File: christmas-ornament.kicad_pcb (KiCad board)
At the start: 2 copper layers, 76.2 x 76.2 mm, 14 parts, among them SW1 SW_SPDT

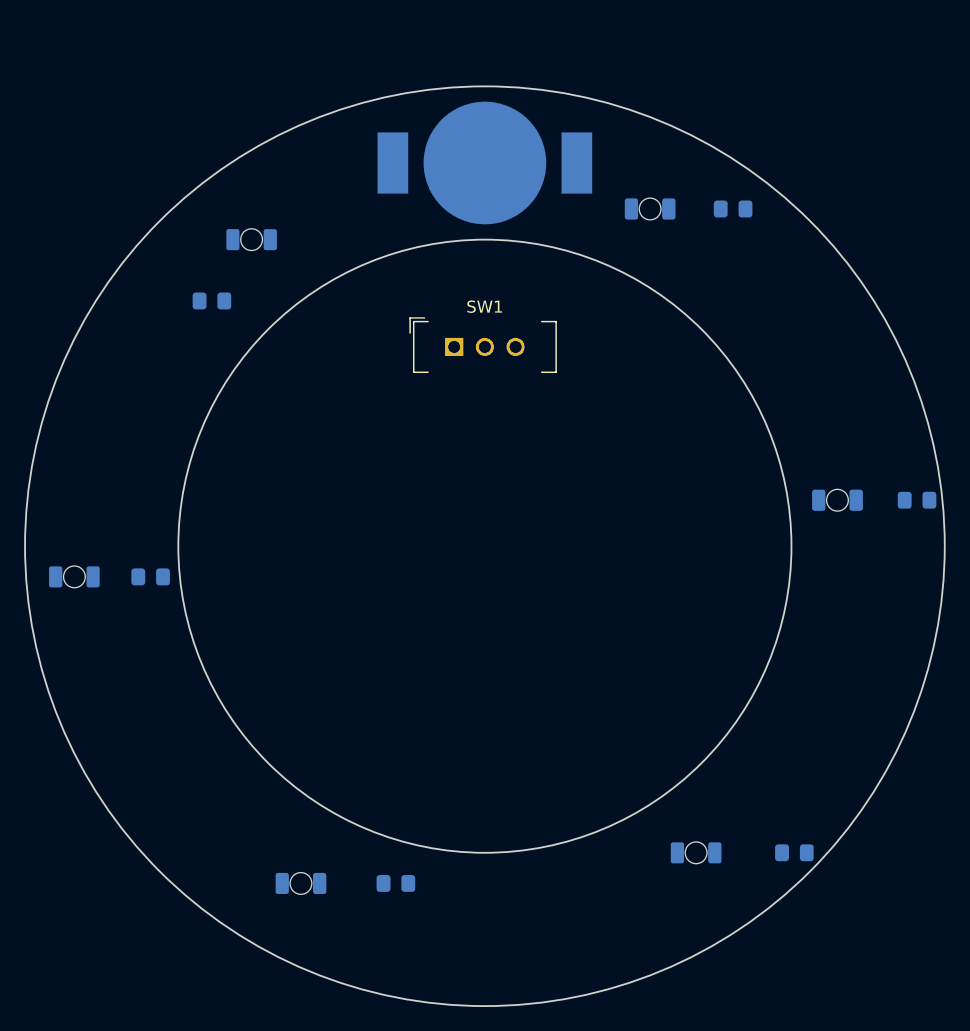
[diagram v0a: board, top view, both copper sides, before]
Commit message: use the square hole led footprint
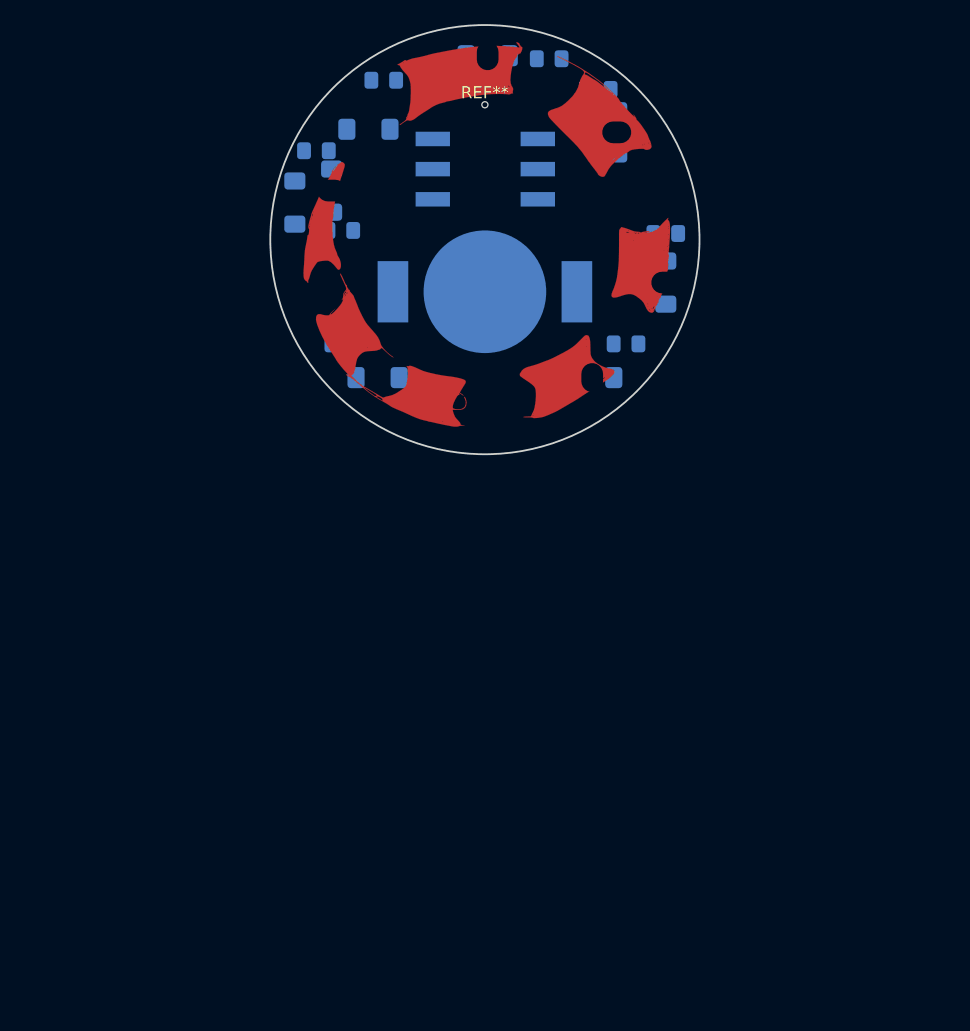
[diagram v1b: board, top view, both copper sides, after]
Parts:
- added D7: LED, salvation:LED_1206_ReverseMountSquare1.5mm_HandSolder, B.Cu at (161.3, 113.0)
- added D8: LED, salvation:LED_1206_ReverseMountSquare1.5mm_HandSolder, B.Cu at (143.5, 113.0)
- added G***: LOGO, salvation:snek, F.Cu at (152.4, 101.6)
- added R7: 68, Resistor_SMD:R_0805_2012Metric_Pad1.15x1.40mm_HandSolder, B.Cu at (164.1, 110.2)
- added R8: 68, Resistor_SMD:R_0805_2012Metric_Pad1.15x1.40mm_HandSolder, B.Cu at (140.7, 110.2)
- added REF**: wire_hole, salvation:wire_hole, F.Cu at (152.4, 90.4)
- D1, D2, D3, D4, D5, D6: footprint salvation:LED_1206_3216Metric_ReverseMount_Hole1.8x2.4mm -> salvation:LED_1206_ReverseMountSquare1.5mm_HandSolder
- SW1: footprint salvation:SW_EG1218_SPDT -> salvation:smd_spdt; moved to B.Cu
- moved R4 68.9 mm to (157.7, 86.6), turned to 180 degrees
- moved D4 68.3 mm to (152.6, 86.4)
- moved R5 67.9 mm to (161.8, 89.2), turned to 180 degrees
- moved D5 67.5 mm to (163.3, 92.7), turned to 90 degrees
- moved R3 56.2 mm to (144.0, 88.4)
- moved D6 54.7 mm to (167.4, 105.2), turned to 90 degrees
- moved R6 51.3 mm to (167.4, 101.1)
- moved D3 49.5 mm to (142.7, 92.5)
- moved R2 32.6 mm to (140.5, 100.8)
- moved D2 26.4 mm to (139.7, 97.5), turned to 90 degrees
- moved R1 15.2 mm to (138.4, 94.2)
- moved SW1 14.7 mm to (152.4, 95.8), turned to 90 degrees
- moved BT1 10.7 mm to (152.4, 105.9)
- moved D1 4.72 mm to (136.7, 98.5), turned to 90 degrees
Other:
- board size 76.2 x 76.2 mm -> 35.6 x 35.6 mm
- board text added: "LOOK"
- board text added: "STOP"
- board text added: "THINK"
